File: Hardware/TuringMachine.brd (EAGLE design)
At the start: 107 x 101.6 mm, 96 parts, among them IC1 TL072P, IC11 78L09, IC12 78L09, IC6 TL072P, IC7 TL072P, T1 2N3904

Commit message: routing
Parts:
- removed IC1, IC6: TL072P, TomW:DIL08
- added U1: TL074_, MusicThingModular:DIL14
- moved D2 127.9 mm to (21.6, 29.2), turned to 0 degrees
- moved R3 127.8 mm to (21.6, 24.1), turned to 0 degrees
- moved R7 121.6 mm to (21.6, 36.8)
- moved C16 120.7 mm to (21.6, 26.7)
- moved R9 115.5 mm to (21.6, 39.4), turned to 0 degrees
- moved R27 109.6 mm to (21.6, 21.6), turned to 0 degrees
- moved IC7 107.4 mm to (35.6, 43.2), turned to 180 degrees
- moved C13 104.1 mm to (29.2, 43.2)
- moved C17 100.3 mm to (35.6, 33.0), turned to 0 degrees
- moved R26 97.9 mm to (35.6, 35.6), turned to 0 degrees
- moved C14 94.3 mm to (41.9, 43.2)
- moved R4 83.2 mm to (74.9, 6.35), turned to 90 degrees
- moved C7 75.8 mm to (49.5, 6.35), turned to 90 degrees
- moved C8 70.2 mm to (69.8, 6.35), turned to 90 degrees
- moved R15 57.3 mm to (31.8, 90.2)
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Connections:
- net N$29 renamed +9V_1
- net N$38 renamed +9V_2
- new net N$17: R16.2, SWITCH_IC.10, SWITCH_IC.2
- net +12V_FRONT: now also R29.2, U1.4; no longer IC1.8, IC6.8, R29.1
- net -12V_FRONT: now also U1.11; no longer IC1.4, IC6.4
- net B1_BACK: now also AND_2.8, BUFFER2.9, R14.1; no longer AND_2.12, BUFFER2.14, R14.2
- net B2_BACK: now also AND_2.13; no longer AND_2.9
- net B3_BACK: now also AND_2.5, BUFFER2.7; no longer AND_2.1, BUFFER2.3
- net B4_BACK: now also AND_2.1; no longer AND_2.5
- net B8_BACK: now also BUFFER1.5; no longer BUFFER1.3
- net BUFFCLK2_BACK: now also BUFFER1.2; no longer BUFFER2.10
- net BUFFCLK_BACK: now also AND_2.12, AND_2.9, BUFFER2.2; no longer AND_2.13, AND_2.8, BUFFER2.6
- net CLOCK_BACK: now also BUFFER1.3, BUFFER2.3; no longer BUFFER2.7, BUFFER2.9
- net CLOCK_FRONT: now also R13.2; no longer CLK.A
- net GATE1: now also BUFFER2.10; no longer BUFFER2.15
- net GATE3: now also BUFFER2.6; no longer BUFFER2.2
- net GATE8: now also BUFFER1.4; no longer BUFFER1.2
- net GND_BACK: now also BUFFER2.14, C2.1; no longer BUFFER1.5, C2.2
- net GND_FRONT: now also CLK.K, U1.10, U1.3, U1.5; no longer IC1.3, IC1.5, IC6.3, R13.1
- net N$1: now also U1.14; no longer IC6.7
- net N$15: now also CLK.A, R13.1; no longer CLK.K, R13.2
- net N$16: now also R29.1; no longer R29.2
- net N$21: now also U1.2; no longer IC1.2
- net N$22: now also U1.1; no longer IC1.1
- net N$27: now also U1.6; no longer IC1.6
- net N$28: now also C2.2, R14.2; no longer C2.1, R14.1
- net N$41: now also U1.7; no longer IC1.7
- net N$6: now also U1.9; no longer IC6.2
- net N$7: now also U1.13, U1.8; no longer IC6.1, IC6.6
- net NOISE_FRONT: now also U1.12; no longer IC6.5
- net PULSE1: now also AND_2.10; no longer AND_2.11
- net PULSE2: now also AND_2.11; no longer AND_2.10
- net PULSE3: now also AND_2.4; no longer AND_2.3
- net PULSE4: now also AND_2.3; no longer AND_2.4
- net START_OF_LOOP: no longer R16.2, SWITCH_IC.10, SWITCH_IC.2
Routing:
- net +12V_BACK: track 0.00 -> 211.8 mm, vias 0 -> 6
- net LOOP_CTRL_BACK: track 0.00 -> 114.7 mm
- net N$4: track 0.00 -> 106.8 mm, vias 0 -> 1
- net N$17: track 0.00 -> 104.9 mm, vias 0 -> 2
- net N$45: track 0.00 -> 104.3 mm, vias 0 -> 1
- net -12V_BACK: track 0.00 -> 88.5 mm
- net B5_BACK: track 0.00 -> 67.4 mm, vias 0 -> 2
- net B1_BACK: track 0.00 -> 62.8 mm
- net B3_BACK: track 0.00 -> 59.0 mm
- net B6_BACK: track 0.00 -> 58.7 mm, vias 0 -> 2
- net CLOCK_BACK: track 0.00 -> 56.3 mm
- net B7_BACK: track 0.00 -> 55.3 mm, vias 0 -> 2
- net START_OF_LOOP: track 0.00 -> 46.9 mm
- net B8_BACK: track 0.00 -> 43.6 mm, vias 0 -> 2
- net B2_BACK: track 0.00 -> 43.5 mm
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
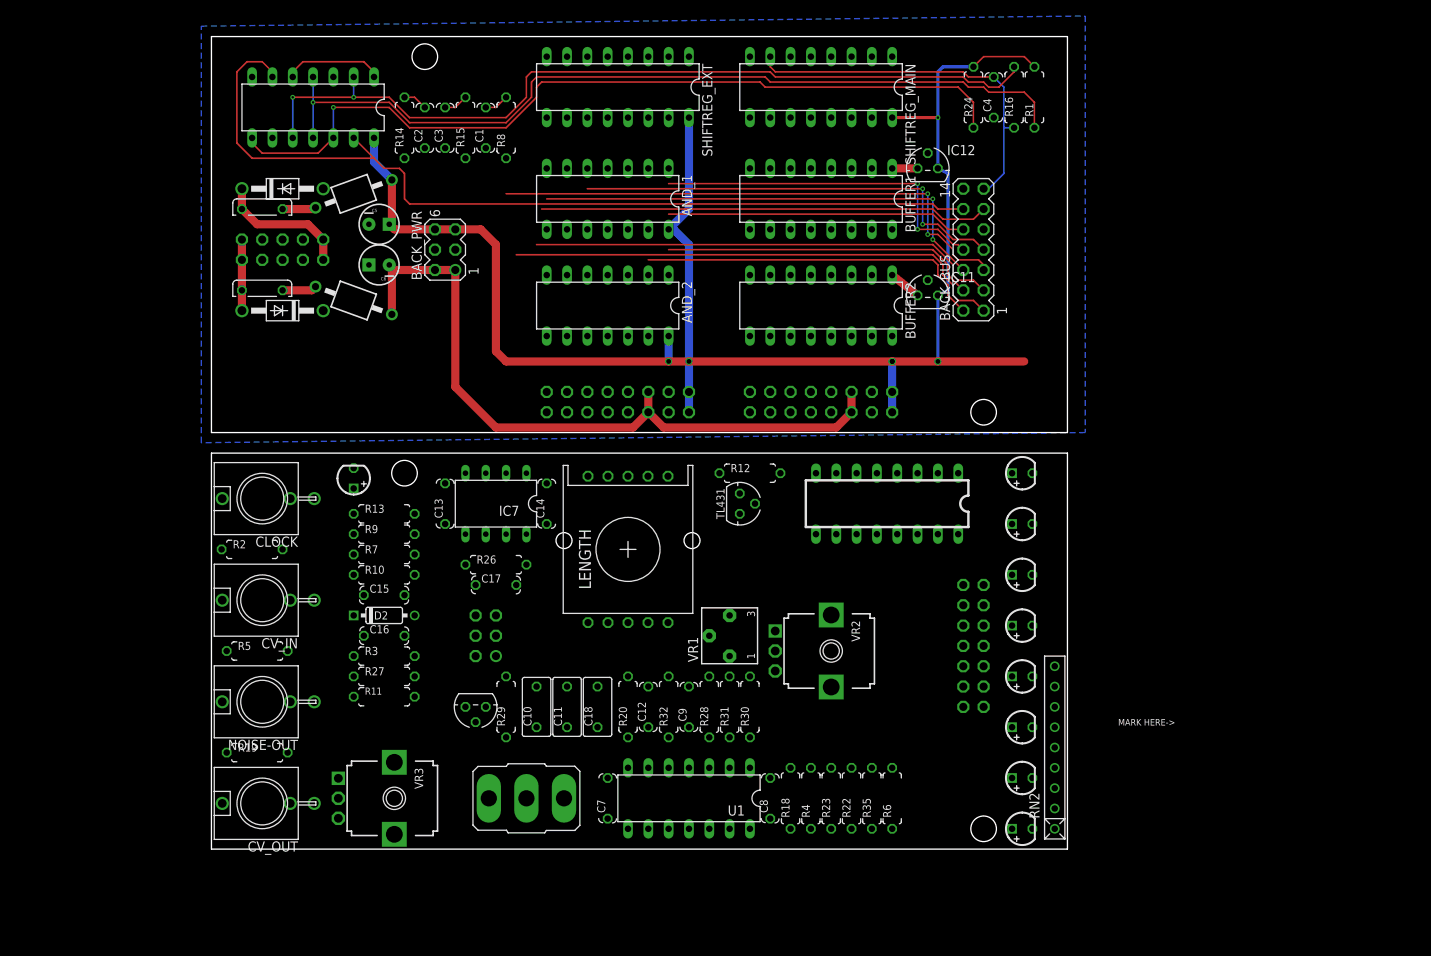
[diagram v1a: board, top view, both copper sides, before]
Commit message: Adding pulse out
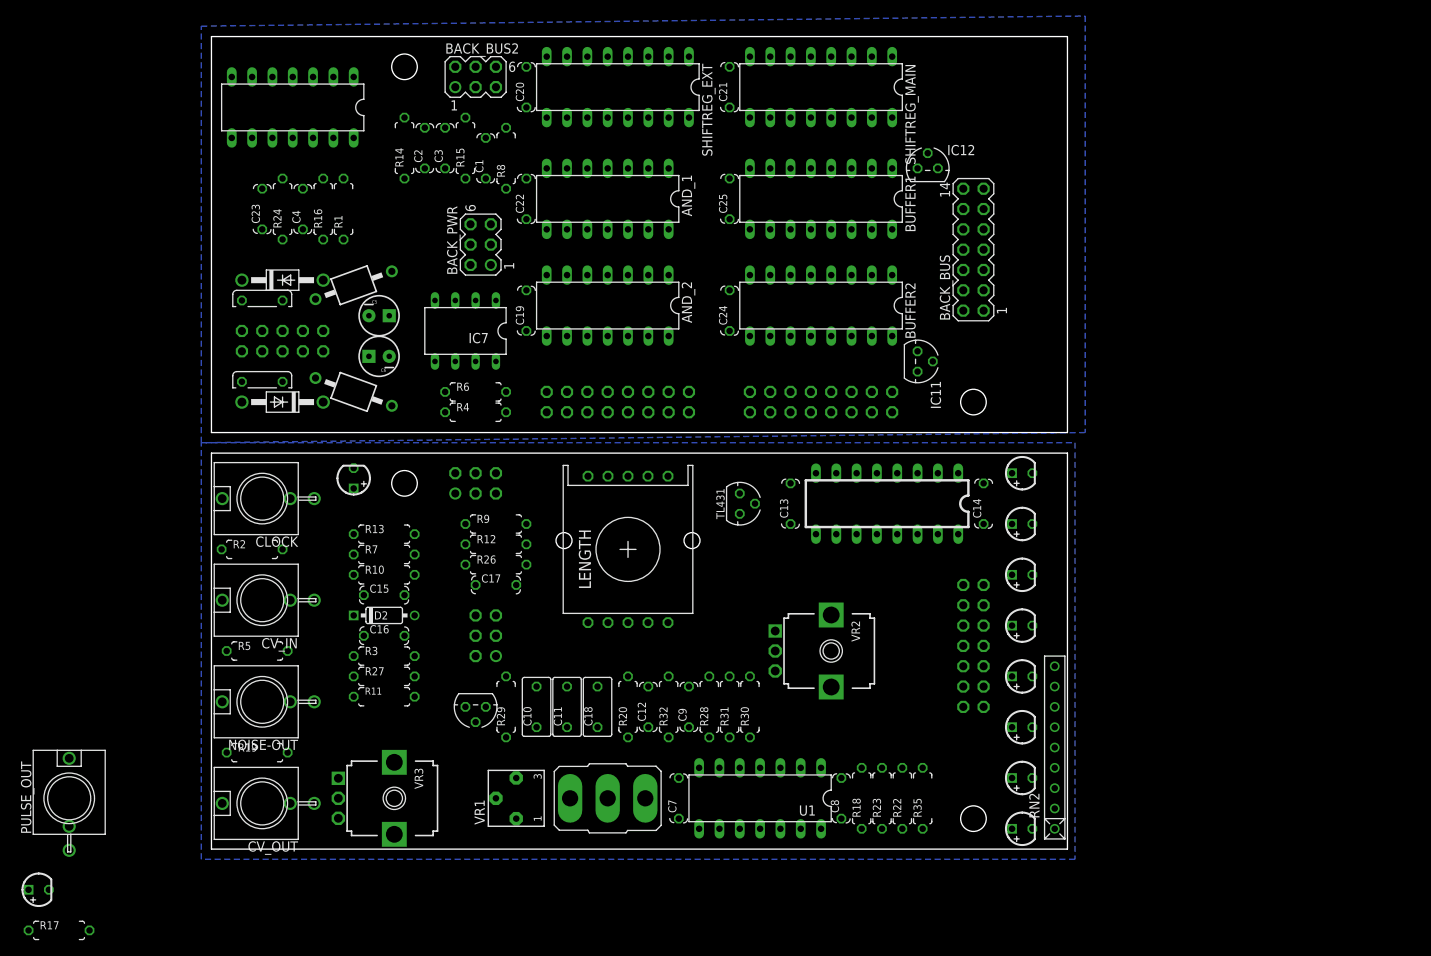
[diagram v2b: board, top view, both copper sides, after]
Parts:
- added BACK_BUS2: (no value), con-lstb:MA03-2
- added C19, C20, C21, C22, C23, C24, C25: 100n, TomW:C050-024X044
- added FRONT_BUS2: (no value), MusicThingModular:MA03-2BACKSIDE
- added PULS1: (no value), TomW:LED3MM
- added PULSE_OUT: THONKICONNNEW, MusicThingModular:WQP-PJ301M-12_JACK
- added R17: 2.2k, TomW:0207/7
- added U$1, U$3, U$4, U$5: (no value), MusicThingModular:MOUNTING_HOLE
- moved C4 87.5 mm to (11.4, 80.0)
- moved R1 87.5 mm to (16.5, 80.0)
- moved R16 87.5 mm to (14.0, 80.0)
- moved R24 87.5 mm to (8.89, 80.0)
- moved R6 72.7 mm to (33.0, 57.1), turned to 0 degrees
- moved R4 63.9 mm to (33.0, 54.6), turned to 0 degrees
- moved C14 54.6 mm to (96.5, 43.2)
- moved C13 43.2 mm to (72.4, 43.2)
- moved VR1 33.5 mm to (38.1, 6.35)
- moved R12 33.0 mm to (35.6, 38.1)
- moved IC7 21.9 mm to (31.8, 64.8)
- moved R9 14.0 mm to (35.6, 40.6)
- moved C5 11.4 mm to (21.0, 66.7)
- moved C6 11.4 mm to (21.0, 61.6)
- moved F1 11.4 mm to (6.35, 68.6)
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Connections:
- new net NOISE_BACK: BACK_BUS2.1, IC7.5
- new net PULSE_OUT_BACK: BACK_BUS.10, BUFFER2.15
- new net PULSE_OUT_FRONT: FRONT_BUS.10, PULSE_OUT.P$3, R17.2
- net +12V_BACK: now also C19.1, C20.1, C21.1, C22.1, C23.1, IC7.8
- net +12V_FRONT: no longer IC7.8
- net +9V_1: now also C24.2
- net +9V_2: now also C25.2
- net -12V_BACK: now also IC7.4
- net -12V_FRONT: no longer IC7.4
- net CLOCK_BACK: now also BACK_BUS.9; no longer BACK_BUS.11
- net CLOCK_FRONT: now also FRONT_BUS.9; no longer FRONT_BUS.11
- net END_OF_LOOP_BACK: now also BACK_BUS2.6; no longer BACK_BUS.14
- net END_OF_LOOP_FRONT: now also FRONT_BUS2.6; no longer FRONT_BUS.14
- net GND_BACK: now also C19.2, C20.2, C21.2, C22.2, C23.2, C24.1, C25.1, IC7.3; no longer BUFFER2.14
- net GND_FRONT: now also PULS1.K, PULSE_OUT.P$1; no longer IC7.3
- net LOOP_CTRL_BACK: now also BACK_BUS2.4, IC7.2, R4.2, R6.2; no longer BACK_BUS.12
- net LOOP_CTRL_FRONT: now also FRONT_BUS2.4, R22.1, R5.2; no longer FRONT_BUS.12, R4.2
- net MAIN_OUT: now also U1.8; no longer IC7.1
- net N$1: now also IC7.7; no longer U1.14
- net N$12: now also U1.13; no longer IC7.6
- net N$13: now also U1.9; no longer IC7.2
- net N$5: now also U1.12; no longer IC7.5
- net N$6: now also PULS1.A, R17.1; no longer R22.1, R5.2, R6.2, U1.9
- net N$7: now also IC7.1, IC7.6; no longer U1.13, U1.8
- net N$8: now also U1.14; no longer IC7.7
- net NOISE_FRONT: now also FRONT_BUS2.1; no longer U1.12
- net PULSE1: now also BUFFER2.14
- net START_OF_LOOP: now also BACK_BUS2.5; no longer BACK_BUS.13
- net STEP_12_BACK: now also BACK_BUS2.3; no longer BACK_BUS.9
- net STEP_12_FRONT: now also FRONT_BUS2.3; no longer FRONT_BUS.9
- net STEP_16_BACK: now also BACK_BUS2.2; no longer BACK_BUS.10
- net STEP_16_FRONT: now also FRONT_BUS2.2; no longer FRONT_BUS.10
- net WRITE_SW_FRONT: now also FRONT_BUS2.5; no longer FRONT_BUS.13
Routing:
- net +12V_BACK: track 211.8 -> 0.00 mm, vias 6 -> 0
- net LOOP_CTRL_BACK: track 114.7 -> 0.00 mm
- net N$4: track 106.8 -> 0.00 mm, vias 1 -> 0
- net N$17: track 104.9 -> 0.00 mm, vias 2 -> 0
- net N$45: track 104.3 -> 0.00 mm, vias 1 -> 0
- net -12V_BACK: track 88.5 -> 0.00 mm
- net B5_BACK: track 67.4 -> 0.00 mm, vias 2 -> 0
- net B1_BACK: track 62.8 -> 0.00 mm
- net B3_BACK: track 59.0 -> 0.00 mm
- net B6_BACK: track 58.7 -> 0.00 mm, vias 2 -> 0
- net CLOCK_BACK: track 56.3 -> 0.00 mm
- net B7_BACK: track 55.3 -> 0.00 mm, vias 2 -> 0
- net START_OF_LOOP: track 46.9 -> 0.00 mm
- net B8_BACK: track 43.6 -> 0.00 mm, vias 2 -> 0
- net B2_BACK: track 43.5 -> 0.00 mm
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- added copper zone on layer 16, net GND_FRONT
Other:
- board text removed: "MARK HERE->"

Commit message: Before board split
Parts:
- moved C16 102.0 mm to (123.2, 35.6)
- moved R11 102.0 mm to (123.2, 27.9)
- moved R27 102.0 mm to (123.2, 30.5)
- moved R3 102.0 mm to (123.2, 33.0)
- moved C17 100.6 mm to (135.9, 40.0)
- moved R10 94.7 mm to (115.6, 45.7)
- moved R12 94.7 mm to (129.5, 49.5)
- moved R13 94.7 mm to (115.6, 50.8)
- moved R26 94.7 mm to (129.5, 47.0)
- moved R7 94.7 mm to (115.6, 48.3)
- moved R9 94.7 mm to (129.5, 52.1)
- moved T1 87.0 mm to (120.0, 17.1)
- moved R29 86.8 mm to (123.2, 9.53), turned to 180 degrees
- moved PULS1 56.8 mm to (28.6, 21.6), turned to 180 degrees
- moved R17 52.6 mm to (20.3, 24.8)
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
